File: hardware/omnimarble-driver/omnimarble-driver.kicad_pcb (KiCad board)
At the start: 4 copper layers, 220 x 150 mm, 178 parts, among them J1 BarrelJack_Horizontal, J10 PinSocket_1x20_P2.54mm_Vertic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, J11 PinHeader_2x13_P2.54mm_Vertic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, J2 TerminalBarrier_1x02_P9.50mm, J3 PinHeader_1x02_P2.54mm_Vertic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, J4 PinHeader_1x03_P2.54mm_Vertic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, J5 TerminalBarrier_1x02_P9.50mm, J6 IDC-Header_2x05_P2.54mm_Verti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, J7 IDC-Header_2x05_P2.54mm_Verti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, J8 JST_XH_B4B-XH-A_1x04_P2.50mm_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, J9 PinSocket_1x20_P2.54mm_Vertic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, K1 Relay_HF3FF_T73, K2 Relay_HF3FF_T73, Q1 SOT-23, Q10 TOLL-8, Q11 TOLL-8, Q12 TOLL-8, Q2 SOT-23, Q3 SOT-23, Q4 SOT-23, Q90 TO-252-2, Q91 TO-252-2, U1 TSOT-23-6, U10 VSSOP-8_2.3x2mm_P0.5mm, U11 SOIC-14_3.9x8.7mm_P1.27mm, U12 SOIC-14_3.9x8.7mm_P1.27mm, U2 SOT-89-3, U3 SOIC-8_3.9x4.9mm_P1.27mm, U4 SOIC-8_3.9x4.9mm_P1.27mm, U5 SOT-23, U6 SOT-353_SC-70-5, U7 SOIC-8_3.9x4.9mm_P1.27mm, U8 SOIC-8_3.9x4.9mm_P1.27mm, U9 TSSOP-8_3x3mm_P0.65mm

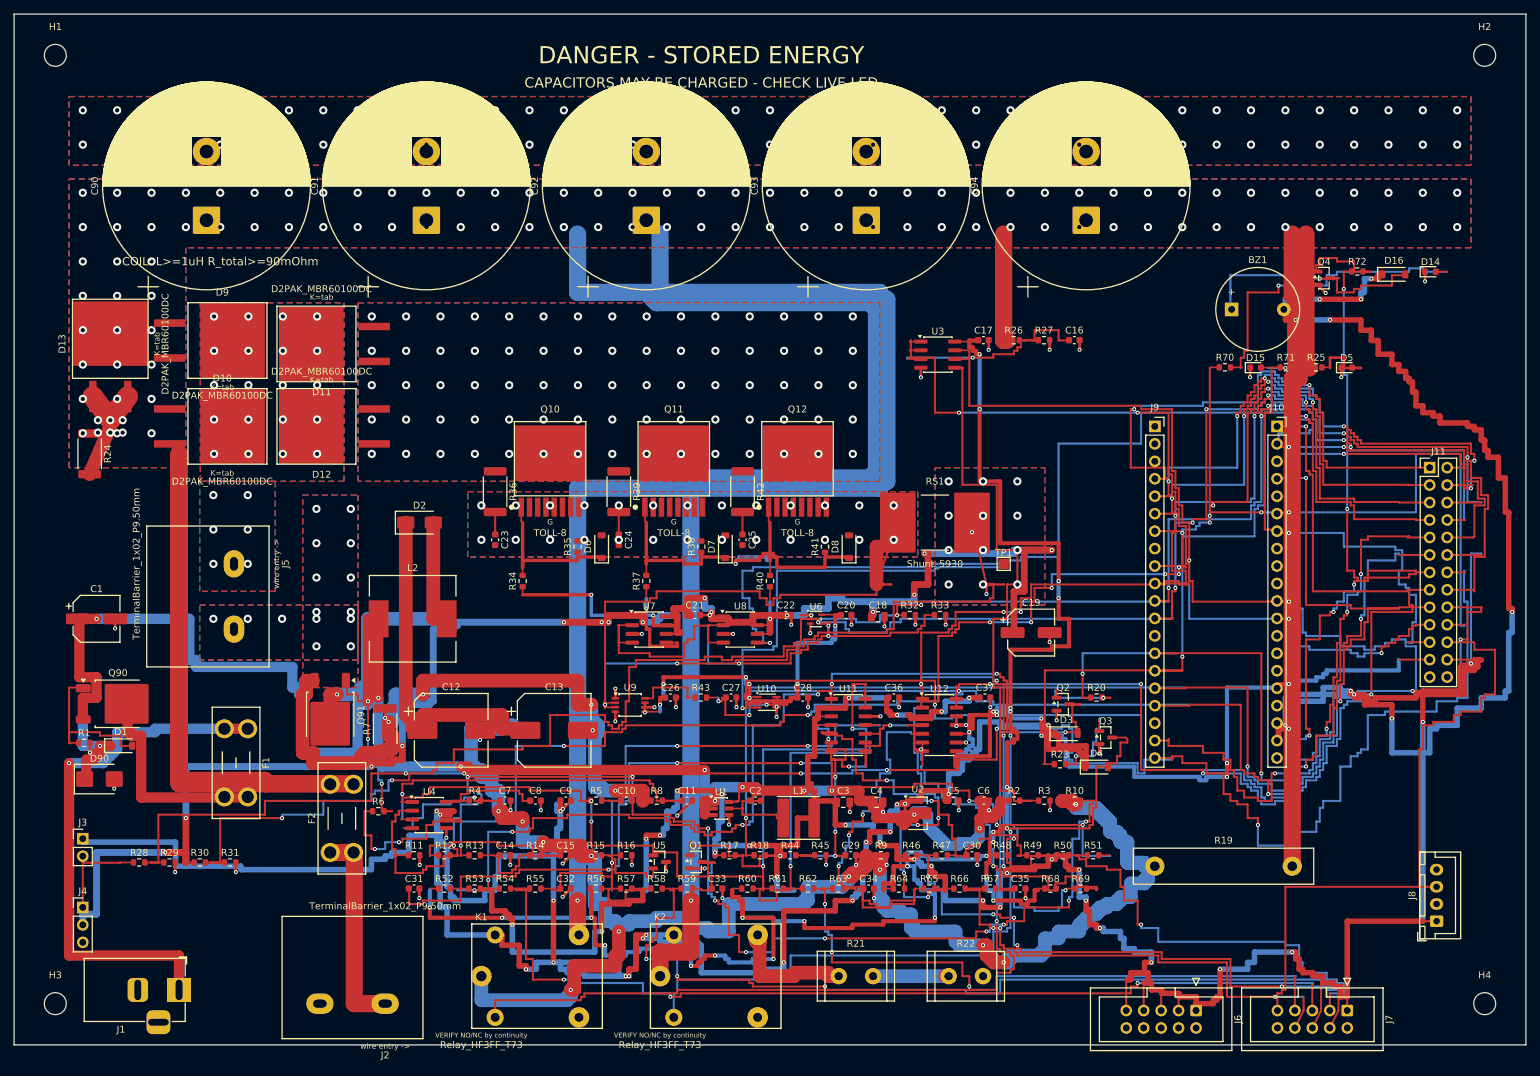
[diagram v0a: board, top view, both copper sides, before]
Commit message: Gate-rail PCB: DRC-clean 224x15mm rail, driver preroute/freerouting flow
- gen_rail_pcb.py: deterministic planar wiring (F/B split lanes),
  station-x assertions to 0.01mm, EMIT/RECV checkboxes, fiducial
- gate-rail DRC: 0 errors, 0 unconnected
- gen_pcb.py: preroute/import-ses/repair phases, LT_POWER inner layers,
  grid-aware SES import, mounting holes with annular pads

Co-Authored-By: Claude Fable 5 <noreply@anthropic.com>
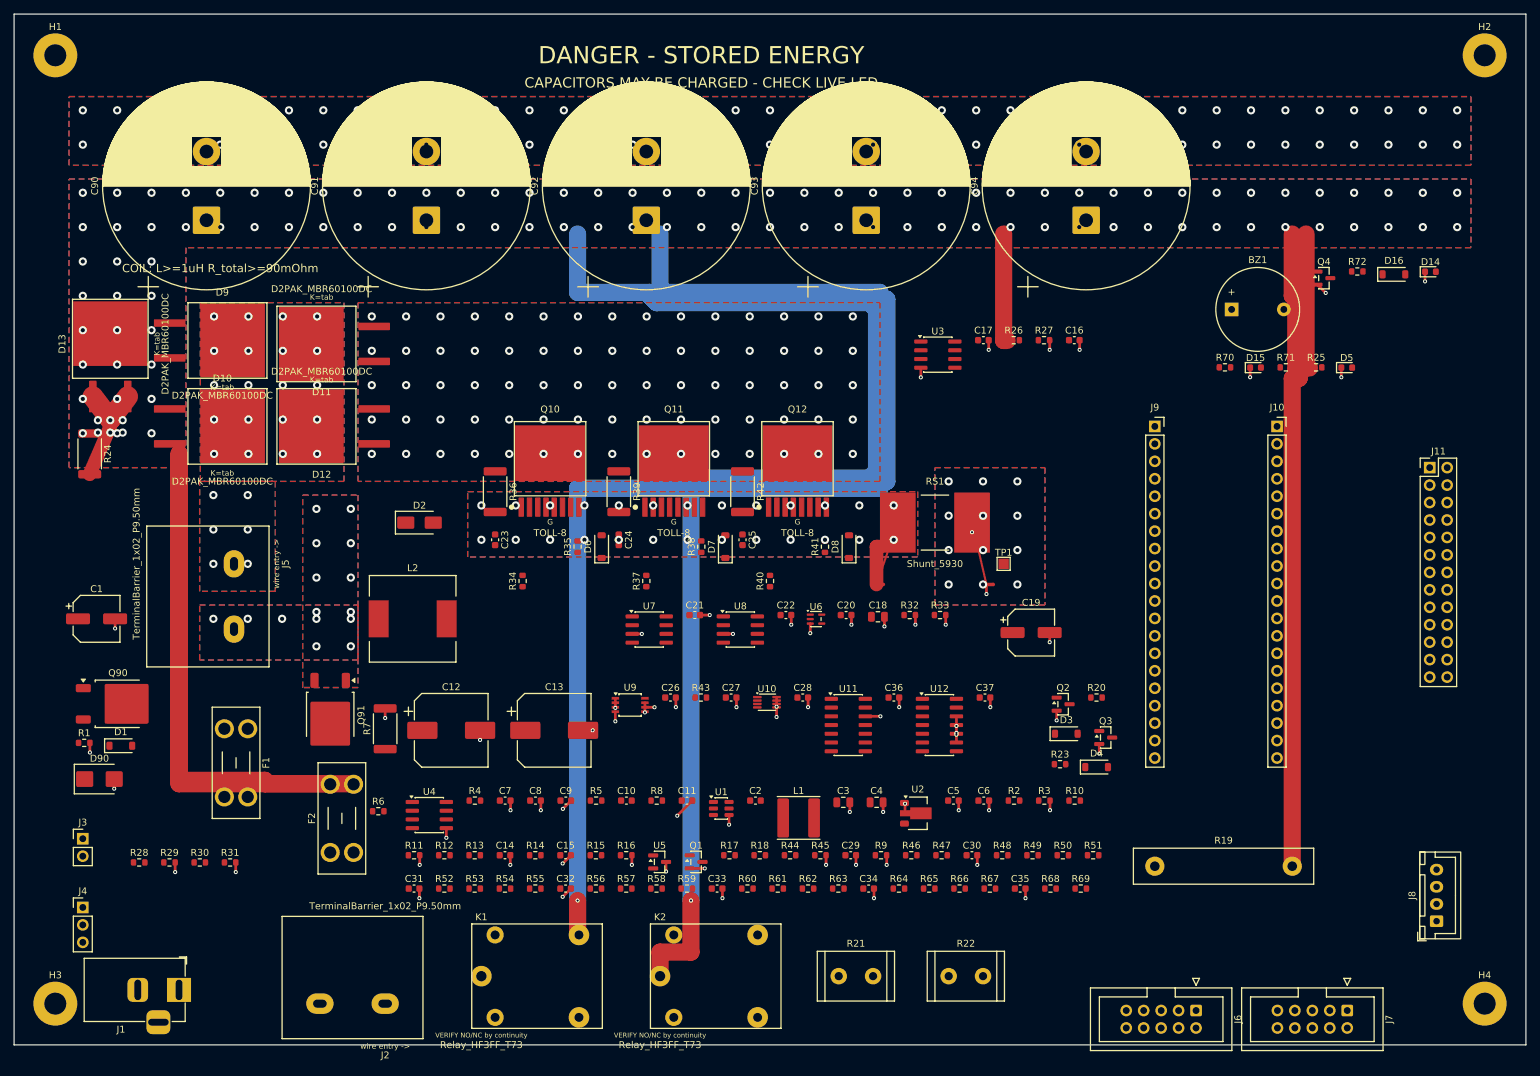
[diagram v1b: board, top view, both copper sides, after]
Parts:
- H1, H2, H3, H4: value MountingHole_3.2mm_M3 -> MountingHole_3.2mm_M3_Pad; footprint MountingHole_3.2mm_M3 -> MountingHole_3.2mm_M3_Pad
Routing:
- net +5V: track 633.5 -> 0.00 mm, vias 40 -> 0
- net 3V3: track 494.0 -> 0.00 mm, vias 40 -> 0
- net +12V: track 357.8 -> 0.00 mm, vias 17 -> 0
- net VBOOST: track 331.8 -> 0.00 mm, vias 13 -> 0
- net ARM_SENSE: track 288.1 -> 0.00 mm, vias 8 -> 0
- net ESTOP_SENSE: track 285.8 -> 0.00 mm, vias 6 -> 0
- net +24V: track 271.7 -> 0.00 mm, vias 12 -> 0
- net +12V_SW: track 255.9 -> 0.00 mm, vias 15 -> 0
- net VSET_PWM: track 234.3 -> 0.00 mm, vias 6 -> 0
- net GATE6: track 222.3 -> 0.00 mm, vias 11 -> 0
- net ADC_SDO: track 197.7 -> 0.00 mm, vias 7 -> 0
- net ADC_CS: track 197.2 -> 0.00 mm, vias 3 -> 0
- net GATE5: track 189.8 -> 0.00 mm, vias 16 -> 0
- net ADC_SCK: track 188.8 -> 0.00 mm, vias 3 -> 0
- net BST_FB: track 187.9 -> 0.00 mm, vias 11 -> 0
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
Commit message: Driver PCB checkpoint: placement + power/pulse copper + planes
Board state: all 178 footprints placed in functional zones (collision-
free), 20 zones filled (In1/In2 solid GND planes at 91%, F/B pulse
pours at 25% leaving 75% open for signal routing), pulse-path copper +
Kelvin + via stitching, GND/pulse/power nets carried by planes. DSN
re-exported from the board via pcbnew's own ExportSpecctraDSN (the
fork's hand-rolled DSN exporter was broken - only emitted 13 stub nets).

Signal-layer autorouting still open: freerouting v2.1.0 headless
(--gui.enabled=false --router.max_threads=8) engages multi-thread but
chokes with target_shape-null NPEs trying to maze-route the GND/pulse
PLANE nets (should via-stitch, not route). Next: exclude plane nets
from the routable network so it only routes the ~70 real signal nets.

Co-Authored-By: Claude Fable 5 <noreply@anthropic.com>
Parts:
- moved R24 7.00 mm to (18.0, 64.0)
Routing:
- net GND: track 130.5 -> 141.0 mm, vias 172 -> 171
- net VBANK: track 637.2 -> 638.2 mm, vias 102 -> 100
- net SNB3: vias 1 -> 0
- net SNB2: vias 1 -> 0
- net SNB1: vias 1 -> 0
- net SHUNT_HI: vias 22 -> 21
- net QG1: vias 1 -> 0
